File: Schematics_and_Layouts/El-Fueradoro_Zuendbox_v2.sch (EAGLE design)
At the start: 139 parts, among them IC1 MAX202, IC2 MEGA168P/328P, IC6 74HC595N, IC7 74HC595N, IC8 LM1086IT-3.3, Q1 9.8304, Q10 IRF3708, Q11 IRF3708, Q12 IRF3708, Q13 IRF3708, Q14 IRF3708, Q15 IRF3708, Q16 IRF3708, Q17 IRF3708, Q18 BC337, Q19 IRF4905, Q2 IRF3708, Q3 IRF3708, Q4 IRF3708, Q5 IRF3708, Q6 IRF3708, Q7 IRF3708, Q8 IRF3708, Q9 IRF3708, T1 BC337, T2 BC 327

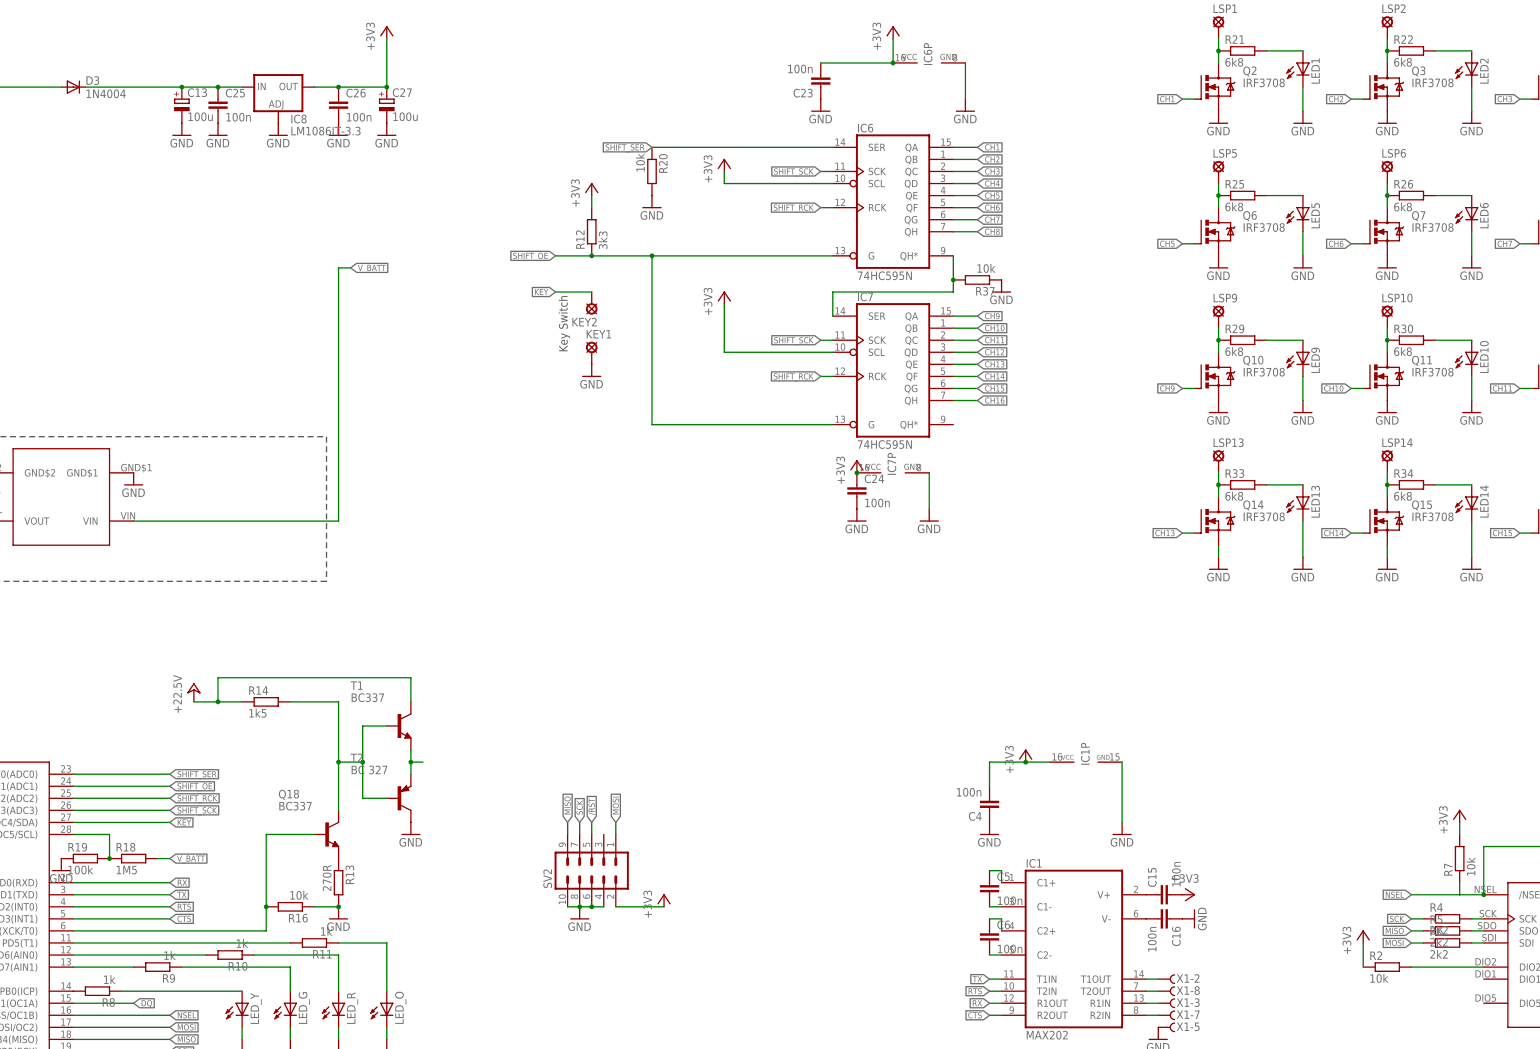
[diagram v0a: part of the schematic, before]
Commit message: Angleichung von Handbuch und Layouts
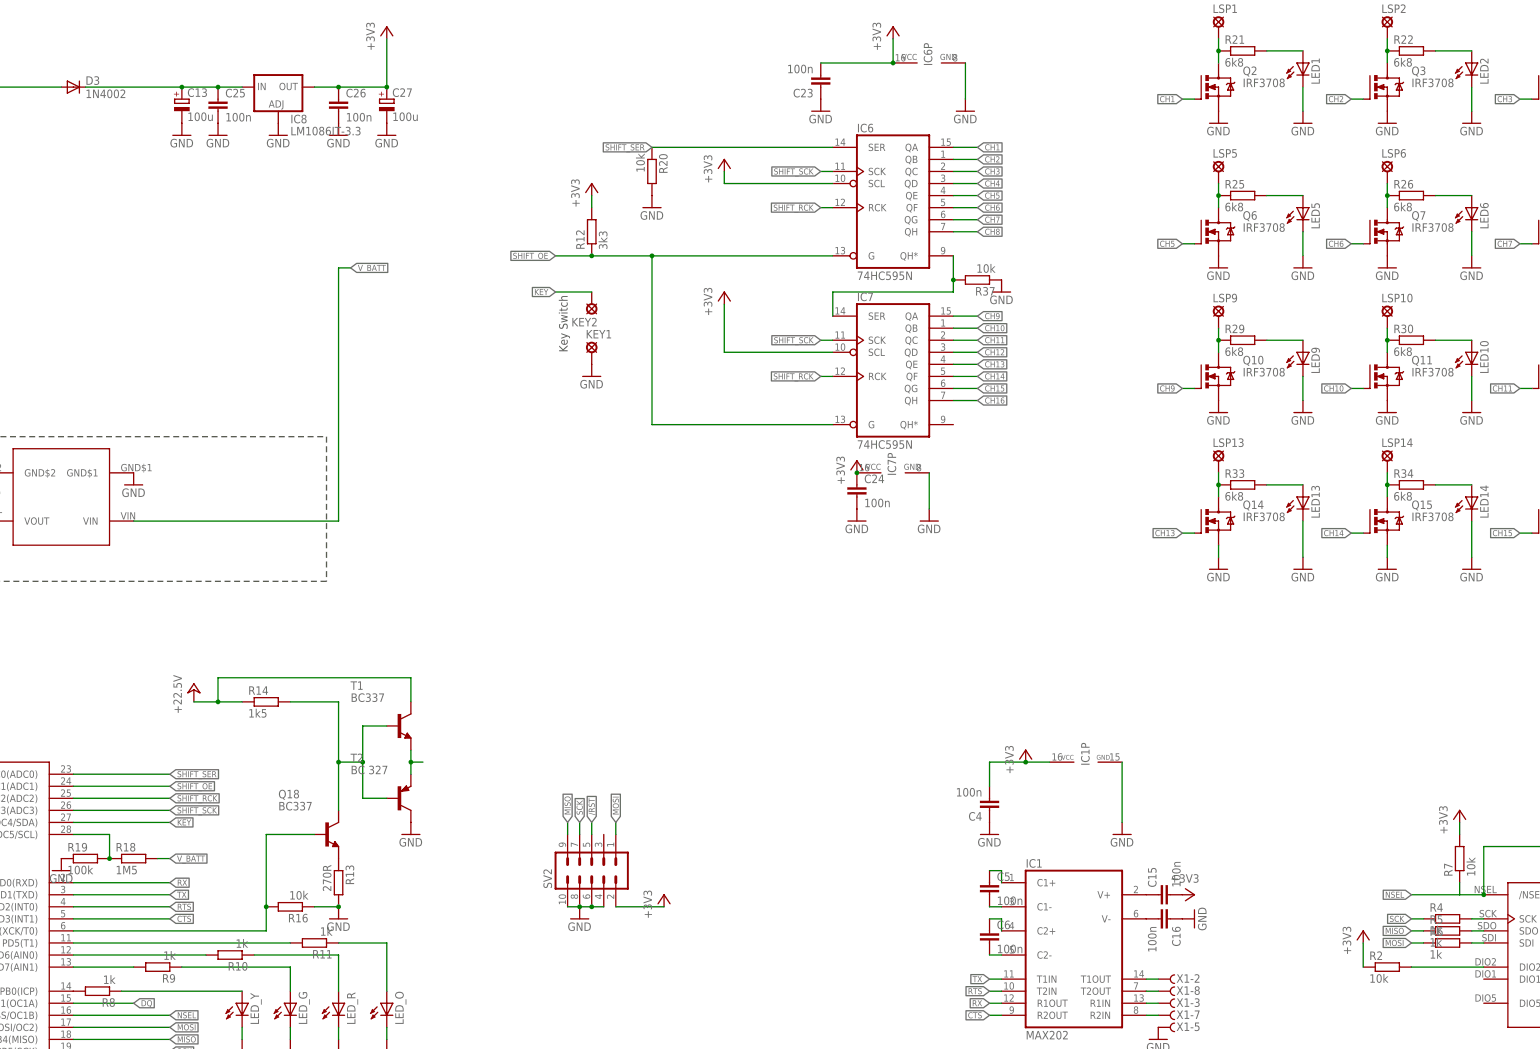
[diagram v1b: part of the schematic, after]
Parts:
- D3: value 1N4004 -> 1N4002
- R4, R5, R6: value 2k2 -> 1k
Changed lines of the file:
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@@
 <part name="P+3" library="supply1" deviceset="+3V3" device=""/>
 <part name="P+7" library="supply1" deviceset="+3V3" device=""/>
-<part name="R4" library="rcl" deviceset="R-EU_" device="0207/10" value="2k2"/>
-<part name="R5" library="rcl" deviceset="R-EU_" device="0207/10" value="2k2"/>
-<part name="R6" library="rcl" deviceset="R-EU_" device="0207/10" value="2k2"/>
+<part name="R4" library="rcl" deviceset="R-EU_" device="0207/10" value="1k"/>
+<part name="R5" library="rcl" deviceset="R-EU_" device="0207/10" value="1k"/>
+<part name="R6" library="rcl" deviceset="R-EU_" device="0207/10" value="1k"/>
 <part name="GND6" library="supply1" deviceset="GND" device=""/>
 <part name="GND8" library="supply1" deviceset="GND" device=""/>
@@
 <part name="GND78" library="supply1" deviceset="GND" device=""/>
 <part name="+3V1" library="supply1" deviceset="+3V3" device=""/>
-<part name="D3" library="diode" deviceset="1N4004" device=""/>
+<part name="D3" library="diode" deviceset="1N4004" device="" value="1N4002"/>
 <part name="U$2" library="fp" deviceset="DS18B20" device=""/>
 <part name="R38" library="rcl" deviceset="R-EU_" device="0207/10" value="3k3"/>
